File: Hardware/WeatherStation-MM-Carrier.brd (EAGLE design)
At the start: 67.3 x 58.4 mm, 156 parts, among them J11 microSD, J13 RJ11 - WIND, J15 MICROMOD-2222-C, J2 JTAG, J3 QWIIC_RIGHT_ANGLE, J7 RJ11 - RAIN, U1 BME280, U2 VEML6075, U3 AS3935, U5 AP7361C-33FGEUDFN-8

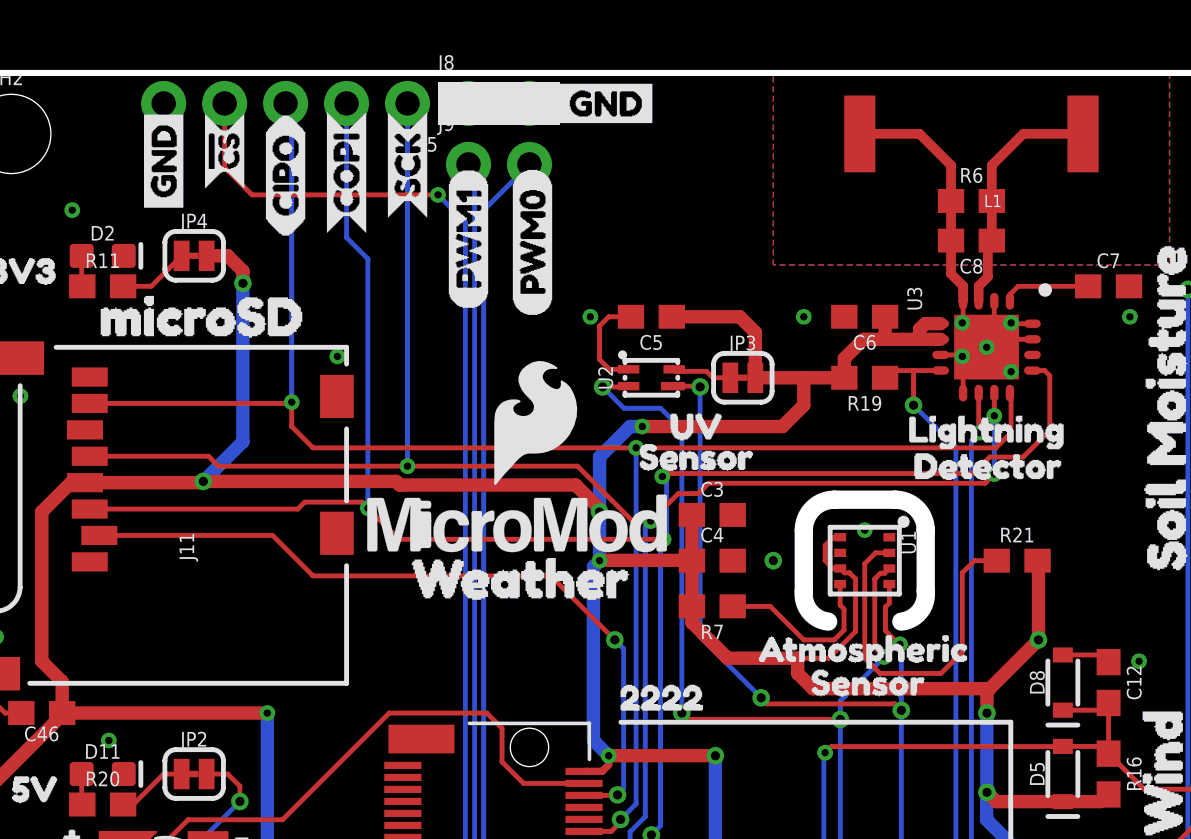
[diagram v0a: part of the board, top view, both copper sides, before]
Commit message: Moved silkscreen
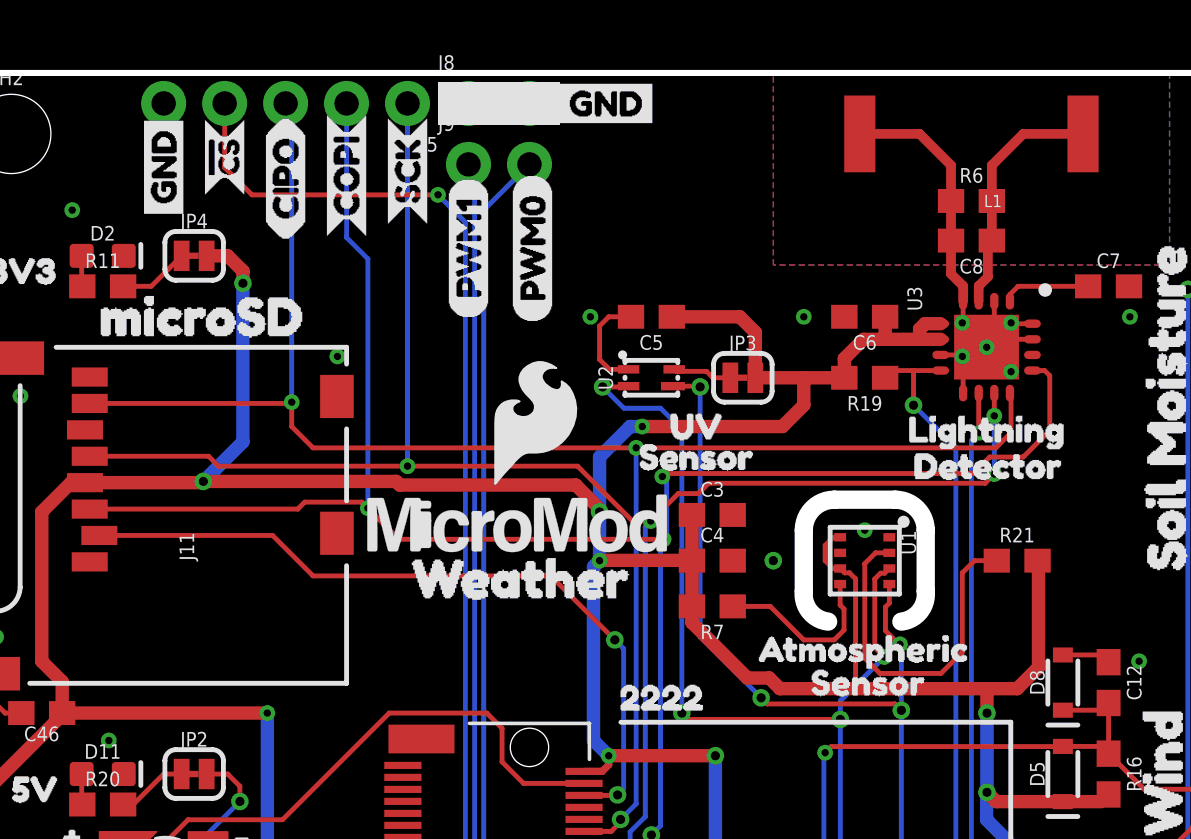
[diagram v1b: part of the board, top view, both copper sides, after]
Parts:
- removed U$26: (no value), buzzard_labels (11):VIN#31
- R8: value 1k -> 3.3k
- moved U$61 0.38 mm to (21.6, 48.1)
- moved U$10 0.25 mm to (11.4, 53.1)
- moved U$6 0.25 mm to (8.89, 52.1)
- moved U$60 0.25 mm to (24.3, 48.0)
- moved U$9 0.25 mm to (19.1, 52.1)
- moved U$7 0.13 mm to (16.5, 51.6)
- moved U$27 0.13 mm to (14.0, 51.4)
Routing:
- net 3.3V: track 274.1 -> 273.9 mm, vias 14 -> 13
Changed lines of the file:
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@@
 <layer number="46" name="Milling" color="3" fill="1" visible="no" active="yes"/>
 <layer number="47" name="Measures" color="7" fill="1" visible="no" active="yes"/>
-<layer number="48" name="Document" color="7" fill="1" visible="yes" active="yes"/>
+<layer number="48" name="Document" color="7" fill="1" visible="no" active="yes"/>
 <layer number="49" name="Reference" color="7" fill="1" visible="no" active="yes"/>
 <layer number="50" name="dxf" color="7" fill="1" visible="no" active="yes"/>
@@
 <attribute name="VALUE" x="3.937" y="24.13" size="0.6096" layer="27" font="vector" ratio="20" rot="R90" align="top-center"/>
 </element>
-<element name="R8" library="SparkFun-Resistors" package="0603" value="1k" x="5.08" y="24.13" smashed="yes" rot="R270">
+<element name="R8" library="SparkFun-Resistors" package="0603" value="3.3k" x="5.08" y="24.13" smashed="yes" rot="R270">
 <attribute name="NAME" x="5.642" y="24.13" size="0.6096" layer="25" font="vector" ratio="20" rot="R270" align="bottom-center"/>
-<attribute name="PROD_ID" value="RES-07856" x="12.7" y="38.1" size="1.778" layer="27" font="vector" ratio="15" rot="R270" display="off"/>
-<attribute name="VALUE" x="4.518" y="24.13" size="0.6096" layer="27" font="vector" ratio="20" rot="R270" align="top-center"/>
+<attribute name="PROD_ID" value="RES-07851" x="12.7" y="38.1" size="1.778" layer="27" font="vector" ratio="15" rot="R270" display="off"/>
+<attribute name="VALUE" value="3.3k" x="4.518" y="24.13" size="0.6096" layer="27" font="vector" ratio="20" rot="R270" align="top-center"/>
 </element>
 <element name="D7" library="SparkFun-DiscreteSemi" package="SOD-323" value="1A/23V/620mV" x="1.27" y="24.13" smashed="yes" rot="R90">
@@
 <element name="U$2" library="buzzard_labels (9)" package="RESET3" value="" x="13.589" y="0.889" smashed="yes"/>
 <element name="U$5" library="SparkFun-Buzzard" package="MEAS" value="" x="13.589" y="3.683" smashed="yes" rot="MR0"/>
-<element name="U$9" library="SparkFun-Buzzard" package="SCK_O" value="" x="19.05" y="52.324" smashed="yes" rot="R90"/>
-<element name="U$10" library="SparkFun-Buzzard" package="!CS_O" value="" x="11.43" y="53.34" smashed="yes" rot="R90"/>
-<element name="U$6" library="SparkFun-Buzzard" package="GND_P" value="" x="8.89" y="52.324" smashed="yes" rot="R90"/>
+<element name="U$9" library="SparkFun-Buzzard" package="SCK_O" value="" x="19.05" y="52.07" smashed="yes" rot="R90"/>
+<element name="U$10" library="SparkFun-Buzzard" package="!CS_O" value="" x="11.43" y="53.086" smashed="yes" rot="R90"/>
+<element name="U$6" library="SparkFun-Buzzard" package="GND_P" value="" x="8.89" y="52.07" smashed="yes" rot="R90"/>
 <element name="U$11" library="SparkFun-Buzzard" package="GND_P" value="" x="29.718" y="57.15" smashed="yes" rot="MR0"/>
 <element name="U$19" library="buzzard_labels (10)" package="BOOT2" value="" x="20.32" y="0.889" smashed="yes"/>
@@
 <element name="U$53" library="SparkFun-Buzzard" package="GND_P" value="" x="8.89" y="52.324" smashed="yes" rot="MR90"/>
 <element name="U$55" library="buzzard_labels (9)" package="22229" value="" x="26.962" y="32.39" smashed="yes"/>
-<element name="U$61" library="buzzard_labels (10)" package="PWM10" value="" x="21.59" y="48.514" smashed="yes" rot="R90"/>
+<element name="U$61" library="buzzard_labels (10)" package="PWM10" value="" x="21.59" y="48.133" smashed="yes" rot="R90"/>
 <element name="U$54" library="SparkFun-Buzzard" package="GND_P" value="" x="24.892" y="57.15" smashed="yes"/>
 <element name="H5" library="SparkFun-Hardware" package="STAND-OFF-REFLOW-M2.5" value="STAND-OFF-REFLOW2.5MM_TALL" x="44.2" y="16.3" smashed="yes">
@@
 <element name="U$30" library="buzzard_labels (12)" package="RX25" value="" x="30.48" y="1.524" smashed="yes" rot="MR90"/>
 <element name="U$59" library="buzzard_labels (1)" package="PWM01" value="" x="24.257" y="48.26" smashed="yes" rot="MR90"/>
-<element name="U$60" library="buzzard_labels (1)" package="PWM01" value="" x="24.257" y="48.26" smashed="yes" rot="R90"/>
+<element name="U$60" library="buzzard_labels (1)" package="PWM01" value="" x="24.257" y="48.006" smashed="yes" rot="R90"/>
 <element name="U1" library="SparkFun-Sensors" package="LGA-8-2.5X2.5" value="BME280" x="38.1" y="38.1" smashed="yes" rot="R270">
 <attribute name="NAME" x="39.624" y="39.37" size="0.6096" layer="25" font="vector" ratio="20" rot="R270"/>
@@
 <element name="U$57" library="buzzard_labels (3)" package="GND0" value="" x="60.96" y="42.037" smashed="yes" rot="MR90"/>
 <element name="U$63" library="buzzard_labels (3)" package="SIG1" value="" x="60.96" y="47.498" smashed="yes" rot="MR90"/>
-<element name="U$7" library="buzzard_labels (9)" package="COPI0" value="" x="16.51" y="51.689" smashed="yes" rot="R90"/>
+<element name="U$7" library="buzzard_labels (9)" package="COPI0" value="" x="16.51" y="51.562" smashed="yes" rot="R90"/>
 <element name="U$8" library="buzzard_labels (9)" package="COPI0" value="" x="16.51" y="51.562" smashed="yes" rot="MR90"/>
 <element name="U$69" library="buzzard_labels (10)" package="#0" value="" x="3.81" y="26.67" smashed="yes"/>
@@
 <element name="U$14" library="buzzard_labels (11)" package="BYP0" value="" x="4.445" y="20.32" smashed="yes"/>
 <element name="U$21" library="buzzard_labels (11)" package="3#3V_EN2" value="" x="9.525" y="13.843" smashed="yes" rot="MR0"/>
-<element name="U$26" library="buzzard_labels (11)" package="VIN#31" value="" x="12.827" y="16.383" smashed="yes" rot="MR0"/>
-<element name="U$27" library="buzzard_labels (12)" package="CIPO0" value="" x="13.97" y="51.562" smashed="yes" rot="R90"/>
+<element name="U$27" library="buzzard_labels (12)" package="CIPO0" value="" x="13.97" y="51.435" smashed="yes" rot="R90"/>
 <element name="U$50" library="buzzard_labels (12)" package="CIPO0" value="" x="13.97" y="51.562" smashed="yes" rot="MR90"/>
 </elements>
@@
 <wire x1="37.258" y1="37.592" x2="37.465" y2="37.592" width="0.2032" layer="1"/>
 <wire x1="37.465" y1="37.592" x2="37.719" y2="37.338" width="0.2032" layer="1"/>
-<wire x1="37.719" y1="37.338" x2="37.719" y2="35.14818125" width="0.2032" layer="1"/>
-<wire x1="37.719" y1="35.14818125" x2="36.60681875" y2="34.036" width="0.2032" layer="1"/>
 <wire x1="30.9" y1="35.521" x2="30.9" y2="36.195" width="0.5588" layer="1"/>
-<wire x1="36.60681875" y1="34.036" x2="35.306" y2="34.036" width="0.2032" layer="1"/>
-<wire x1="35.306" y1="34.036" x2="32.385" y2="34.036" width="0.5588" layer="1"/>
-<wire x1="32.385" y1="34.036" x2="30.9" y2="35.521" width="0.5588" layer="1"/>
 <wire x1="30.9" y1="36.195" x2="30.9" y2="38.1" width="0.5588" layer="1"/>
 <wire x1="30.9" y1="38.1" x2="30.9" y2="40.005" width="0.5588" layer="1"/>
@@
 <wire x1="30.8873" y1="38.1127" x2="27.0637" y2="38.1127" width="0.5588" layer="1"/>
 <wire x1="30.8873" y1="38.1127" x2="30.9" y2="38.1" width="0.2032" layer="1"/>
-<wire x1="35.306" y1="34.036" x2="35.306" y2="33.401" width="0.5588" layer="1"/>
-<wire x1="35.941" y1="32.766" x2="35.306" y2="33.401" width="0.5588" layer="1"/>
-<wire x1="45.339" y1="34.798" x2="43.307" y2="32.766" width="0.5588" layer="1"/>
-<wire x1="45.339" y1="34.798" x2="45.339" y2="38.061" width="0.5588" layer="1"/>
+<wire x1="45.339" y1="33.655" x2="44.45" y2="32.766" width="0.5588" layer="1"/>
+<wire x1="45.339" y1="33.655" x2="45.339" y2="38.061" width="0.5588" layer="1"/>
 <wire x1="45.339" y1="38.061" x2="45.3" y2="38.1" width="0.2032" layer="1"/>
-<wire x1="35.941" y1="32.766" x2="43.307" y2="32.766" width="0.5588" layer="1"/>
-<via x="45.339" y="34.798" extent="1-16" drill="0.381"/>
+<wire x1="37.719" y1="32.766" x2="43.307" y2="32.766" width="0.5588" layer="1"/>
+<wire x1="43.307" y1="32.766" x2="44.45" y2="32.766" width="0.5588" layer="1"/>
 <wire x1="45.085" y1="22.98" x2="44.824" y2="22.98" width="0.2032" layer="1"/>
 <wire x1="44.824" y1="22.98" x2="44.069" y2="22.225" width="0.5588" layer="1"/>
@@
 <wire x1="37.25" y1="45.72" x2="37.25" y2="46.521" width="0.5588" layer="1"/>
 <wire x1="35.56" y1="45.72" x2="37.25" y2="45.72" width="0.5588" layer="1"/>
+<wire x1="37.719" y1="37.338" x2="37.719" y2="32.766" width="0.2032" layer="1"/>
+<wire x1="34.5684375" y1="32.766" x2="34.1239375" y2="33.2105" width="0.5588" layer="1"/>
+<wire x1="34.1239375" y1="33.2105" x2="33.2105" y2="33.2105" width="0.5588" layer="1"/>
+<wire x1="37.719" y1="32.766" x2="34.5684375" y2="32.766" width="0.5588" layer="1"/>
+<wire x1="33.2105" y1="33.2105" x2="30.9" y2="35.521" width="0.5588" layer="1"/>
 </signal>
 <signal name="USB_D-">

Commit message: Update WeatherStation-MM-Carrier.brd
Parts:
- moved U$35 5.08 mm to (9.91, 48.3)
- moved U$1 2.84 mm to (3.17, 51.4)
- moved R11 2.84 mm to (3.81, 48.3)
- moved JP4 2.84 mm to (7.62, 49.5)
- moved D2 2.84 mm to (3.81, 49.5)
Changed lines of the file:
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@@
 </class>
 </classes>
-<designrules name="SparkFun-2-layer-TIGHT *">
+<designrules name="SparkFun-2-layer-FAB-LIMIT">
 <description language="en">&lt;b&gt;SparkFun 2 Layer Design Rule Checks - STANDARD/TIGHT/FAB-LIMIT&lt;/b&gt;
 &lt;p&gt;
@@
 <param name="mtCopper" value="0.035mm 0.035mm 0.035mm 0.035mm 0.035mm 0.035mm 0.035mm 0.035mm 0.035mm 0.035mm 0.035mm 0.035mm 0.035mm 0.035mm 0.035mm 0.035mm"/>
 <param name="mtIsolate" value="1.5mm 0.15mm 0.2mm 0.15mm 0.2mm 0.15mm 0.2mm 0.15mm 0.2mm 0.15mm 0.2mm 0.15mm 0.2mm 0.15mm 0.2mm"/>
-<param name="mdWireWire" value="7mil"/>
-<param name="mdWirePad" value="7mil"/>
-<param name="mdWireVia" value="7mil"/>
-<param name="mdPadPad" value="7mil"/>
-<param name="mdPadVia" value="7mil"/>
-<param name="mdViaVia" value="7mil"/>
-<param name="mdSmdPad" value="7mil"/>
-<param name="mdSmdVia" value="7mil"/>
-<param name="mdSmdSmd" value="7mil"/>
+<param name="mdWireWire" value="4mil"/>
+<param name="mdWirePad" value="4mil"/>
+<param name="mdWireVia" value="4mil"/>
+<param name="mdPadPad" value="4mil"/>
+<param name="mdPadVia" value="4mil"/>
+<param name="mdViaVia" value="4mil"/>
+<param name="mdSmdPad" value="4mil"/>
+<param name="mdSmdVia" value="4mil"/>
+<param name="mdSmdSmd" value="4mil"/>
 <param name="mdViaViaSameLayer" value="8mil"/>
 <param name="mnLayersViaInSmd" value="2"/>
-<param name="mdCopperDimension" value="7mil"/>
-<param name="mdDrill" value="7mil"/>
+<param name="mdCopperDimension" value="4mil"/>
+<param name="mdDrill" value="4mil"/>
 <param name="mdSmdStop" value="0mil"/>
-<param name="msWidth" value="7mil"/>
-<param name="msDrill" value="12mil"/>
+<param name="msWidth" value="4mil"/>
+<param name="msDrill" value="6mil"/>
 <param name="msMicroVia" value="9.99mm"/>
 <param name="msBlindViaRatio" value="0.5"/>
@@
 <param name="rvMicroViaOuter" value="0.25"/>
 <param name="rvMicroViaInner" value="0.25"/>
-<param name="rlMinPadTop" value="7mil"/>
+<param name="rlMinPadTop" value="5mil"/>
 <param name="rlMaxPadTop" value="20mil"/>
-<param name="rlMinPadInner" value="7mil"/>
+<param name="rlMinPadInner" value="6mil"/>
 <param name="rlMaxPadInner" value="20mil"/>
-<param name="rlMinPadBottom" value="7mil"/>
+<param name="rlMinPadBottom" value="5mil"/>
 <param name="rlMaxPadBottom" value="20mil"/>
-<param name="rlMinViaOuter" value="7mil"/>
+<param name="rlMinViaOuter" value="5mil"/>
 <param name="rlMaxViaOuter" value="20mil"/>
-<param name="rlMinViaInner" value="7mil"/>
+<param name="rlMinViaInner" value="6mil"/>
 <param name="rlMaxViaInner" value="20mil"/>
 <param name="rlMinMicroViaOuter" value="4mil"/>
@@
 <attribute name="VALUE" x="30.81" y="45.72" size="0.6096" layer="27" font="vector" ratio="20" rot="R90" align="top-center"/>
 </element>
-<element name="JP4" library="SparkFun-Jumpers" package="SMT-JUMPER_2_NC_TRACE_SILK" package3d_urn="urn:adsk.eagle:package:39281/1" value="3V3 LED" x="10.16" y="50.8" smashed="yes">
-<attribute name="NAME" x="10.16" y="51.943" size="0.6096" layer="25" font="vector" ratio="20" align="bottom-center"/>
-<attribute name="VALUE" x="10.16" y="49.657" size="0.6096" layer="27" font="vector" ratio="20" align="top-center"/>
-</element>
-<element name="R11" library="SparkFun-Resistors" package="0603" value="1k" x="6.35" y="49.53" smashed="yes">
-<attribute name="NAME" x="6.35" y="50.292" size="0.6096" layer="25" font="vector" ratio="20" align="bottom-center"/>
-<attribute name="PROD_ID" value="RES-07856" x="6.35" y="49.53" size="1.778" layer="27" font="vector" ratio="15" display="off"/>
-<attribute name="VALUE" x="6.35" y="48.768" size="0.6096" layer="27" font="vector" ratio="20" align="top-center"/>
-</element>
-<element name="D2" library="SparkFun-LED" package="LED-0603" value="RED" x="6.35" y="50.8" smashed="yes">
-<attribute name="NAME" x="6.35" y="51.435" size="0.6096" layer="25" font="vector" ratio="20" align="bottom-center"/>
-<attribute name="PROD_ID" value="DIO-00819" x="6.35" y="50.8" size="1.778" layer="27" font="vector" ratio="15" display="off"/>
-<attribute name="VALUE" x="6.35" y="50.165" size="0.6096" layer="27" font="vector" ratio="20" align="top-center"/>
+<element name="JP4" library="SparkFun-Jumpers" package="SMT-JUMPER_2_NC_TRACE_SILK" package3d_urn="urn:adsk.eagle:package:39281/1" value="3V3 LED" x="7.62" y="49.53" smashed="yes">
+<attribute name="NAME" x="7.62" y="50.673" size="0.6096" layer="25" font="vector" ratio="20" align="bottom-center"/>
+<attribute name="VALUE" x="7.62" y="48.387" size="0.6096" layer="27" font="vector" ratio="20" align="top-center"/>
+</element>
+<element name="R11" library="SparkFun-Resistors" package="0603" value="1k" x="3.81" y="48.26" smashed="yes">
+<attribute name="NAME" x="3.81" y="49.022" size="0.6096" layer="25" font="vector" ratio="20" align="bottom-center"/>
+<attribute name="PROD_ID" value="RES-07856" x="3.81" y="48.26" size="1.778" layer="27" font="vector" ratio="15" display="off"/>
+<attribute name="VALUE" x="3.81" y="47.498" size="0.6096" layer="27" font="vector" ratio="20" align="top-center"/>
+</element>
+<element name="D2" library="SparkFun-LED" package="LED-0603" value="RED" x="3.81" y="49.53" smashed="yes">
+<attribute name="NAME" x="3.81" y="50.165" size="0.6096" layer="25" font="vector" ratio="20" align="bottom-center"/>
+<attribute name="PROD_ID" value="DIO-00819" x="3.81" y="49.53" size="1.778" layer="27" font="vector" ratio="15" display="off"/>
+<attribute name="VALUE" x="3.81" y="48.895" size="0.6096" layer="27" font="vector" ratio="20" align="top-center"/>
 </element>
 <element name="C5" library="SparkFun-Capacitors" package="0603" value="0.1uF" x="29.21" y="48.26" smashed="yes" rot="R180">
@@
 <element name="U$16" library="buzzard_labels (3)" package="WEATHER4" value="" x="17.907" y="37.338" smashed="yes"/>
 <element name="LOGO1" library="SparkFun-Aesthetics" package="SFE_LOGO_NAME_FLAME_.2" value="SFE_LOGO_NAME_FLAME.2_INCH" x="33.02" y="25.4" smashed="yes" rot="MR0"/>
-<element name="U$35" library="buzzard_labels (4)" package="MICROSD0" value="" x="4.826" y="48.26" smashed="yes"/>
+<element name="U$35" library="buzzard_labels (4)" package="MICROSD0" value="" x="9.906" y="48.26" smashed="yes"/>
 <element name="U$43" library="buzzard_labels (4)" package="SWD1" value="" x="11.43" y="25.4" smashed="yes"/>
-<element name="U$1" library="buzzard_labels (5)" package="3V31" value="" x="0.635" y="50.165" smashed="yes"/>
+<element name="U$1" library="buzzard_labels (5)" package="3V31" value="" x="3.175" y="51.435" smashed="yes"/>
 <element name="U$18" library="buzzard_labels (5)" package="5V0" value="" x="1.651" y="28.575" smashed="yes"/>
 <element name="JP3" library="SparkFun-Jumpers" package="SMT-JUMPER_2_NC_TRACE_SILK" package3d_urn="urn:adsk.eagle:package:39281/1" value="UV" x="33.02" y="45.72" smashed="yes">
@@
 <wire x1="48.895" y1="9.01" x2="43.949" y2="9.01" width="0.5588" layer="1"/>
 <wire x1="43.949" y1="9.01" x2="42.926" y2="10.033" width="0.5588" layer="1"/>
-<wire x1="10.6807" y1="50.8" x2="11.557" y2="50.8" width="0.5588" layer="1"/>
-<wire x1="12.192" y1="50.165" x2="12.192" y2="49.657" width="0.5588" layer="1"/>
-<via x="12.192" y="49.657" extent="1-16" drill="0.381"/>
-<wire x1="12.192" y1="49.657" x2="12.192" y2="43.053" width="0.5588" layer="16"/>
-<wire x1="12.192" y1="43.053" x2="10.541" y2="41.402" width="0.5588" layer="16"/>
+<wire x1="10.922" y1="49.657" x2="10.795" y2="49.53" width="0.5588" layer="1"/>
+<wire x1="10.795" y1="49.53" x2="8.1407" y2="49.53" width="0.5588" layer="1"/>
+<via x="10.922" y="49.657" extent="1-16" drill="0.381"/>
+<wire x1="10.922" y1="49.657" x2="10.922" y2="41.783" width="0.5588" layer="16"/>
+<wire x1="10.922" y1="41.783" x2="10.541" y2="41.402" width="0.5588" layer="16"/>
 <via x="10.541" y="41.402" extent="1-16" drill="0.381"/>
-<wire x1="11.557" y1="50.8" x2="12.192" y2="50.165" width="0.5588" layer="1"/>
 <wire x1="10.541" y1="41.402" x2="18.57144375" y2="41.402" width="0.5588" layer="1"/>
 <wire x1="18.57144375" y1="41.402" x2="18.72384375" y2="41.2496" width="0.5588" layer="1"/>
@@
 <contactref element="R11" pad="2"/>
 <contactref element="JP4" pad="1"/>
-<wire x1="8.3693" y1="49.53" x2="9.6393" y2="50.8" width="0.2032" layer="1"/>
-<wire x1="7.2" y1="49.53" x2="8.3693" y2="49.53" width="0.2032" layer="1"/>
+<wire x1="5.8293" y1="48.26" x2="7.0993" y2="49.53" width="0.2032" layer="1"/>
+<wire x1="4.66" y1="48.26" x2="5.8293" y2="48.26" width="0.2032" layer="1"/>
 </signal>
 <signal name="N$6">
 <contactref element="D2" pad="A"/>
 <contactref element="R11" pad="1"/>
-<wire x1="5.473" y1="50.8" x2="5.473" y2="49.557" width="0.2032" layer="1"/>
-<wire x1="5.473" y1="49.557" x2="5.5" y2="49.53" width="0.2032" layer="1"/>
+<wire x1="2.933" y1="49.53" x2="2.933" y2="48.287" width="0.2032" layer="1"/>
+<wire x1="2.96" y1="48.26" x2="2.933" y2="48.287" width="0.2032" layer="1"/>
 </signal>
 <signal name="SOIL_MOIST_SIG">
